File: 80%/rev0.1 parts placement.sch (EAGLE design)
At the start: 205 parts, among them J1 USB-B, SW1 CHERRY_MX, SW10 CHERRY_MX, SW11 CHERRY_MX, SW12 CHERRY_MX, SW13 CHERRY_MX, SW14 CHERRY_MX, SW15 CHERRY_MX, SW16 CHERRY_MX, SW17 CHERRY_MX, SW18 CHERRY_MX, SW19 CHERRY_MX, SW2 CHERRY_MX, SW20 CHERRY_MX, SW21 CHERRY_MX, SW22 CHERRY_MX, SW23 CHERRY_MX, SW24 CHERRY_MX, SW25 CHERRY_MX, SW26 CHERRY_MX, SW27 CHERRY_MX, SW28 CHERRY_MX, SW29 CHERRY_MX, SW3 CHERRY_MX, SW30 CHERRY_MX, SW31 CHERRY_MX, SW32 CHERRY_MX, SW33 CHERRY_MX, SW34 CHERRY_MX, SW35 CHERRY_MX, SW36 CHERRY_MX, SW37 CHERRY_MX, SW38 CHERRY_MX, SW39 CHERRY_MX, SW4 CHERRY_MX, SW40 CHERRY_MX, SW41 CHERRY_MX, SW42 CHERRY_MX, SW43 CHERRY_MX, SW44 CHERRY_MX, SW45 CHERRY_MX, SW46 CHERRY_MX, SW47 CHERRY_MX, SW48 CHERRY_MX, SW49 CHERRY_MX, SW5 CHERRY_MX, SW50 CHERRY_MX, SW51 CHERRY_MX, SW52 CHERRY_MX, SW53 CHERRY_MX, SW54 CHERRY_MX, SW55 CHERRY_MX, SW56 CHERRY_MX, SW57 CHERRY_MX, SW58 CHERRY_MX, SW59 CHERRY_MX, SW6 CHERRY_MX, SW60 CHERRY_MX, SW61 CHERRY_MX, SW62 CHERRY_MX, SW63 CHERRY_MX, SW64 CHERRY_MX, SW65 CHERRY_MX, SW66 CHERRY_MX, SW67 CHERRY_MX, SW68 CHERRY_MX, SW69 CHERRY_MX, SW7 CHERRY_MX, SW70 CHERRY_MX, SW71 CHERRY_MX, SW72 CHERRY_MX, SW73 CHERRY_MX, SW74 CHERRY_MX, SW75 CHERRY_MX, SW76 CHERRY_MX, SW77 CHERRY_MX, SW78 CHERRY_MX, SW79 CHERRY_MX, SW8 CHERRY_MX, SW80 CHERRY_MX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

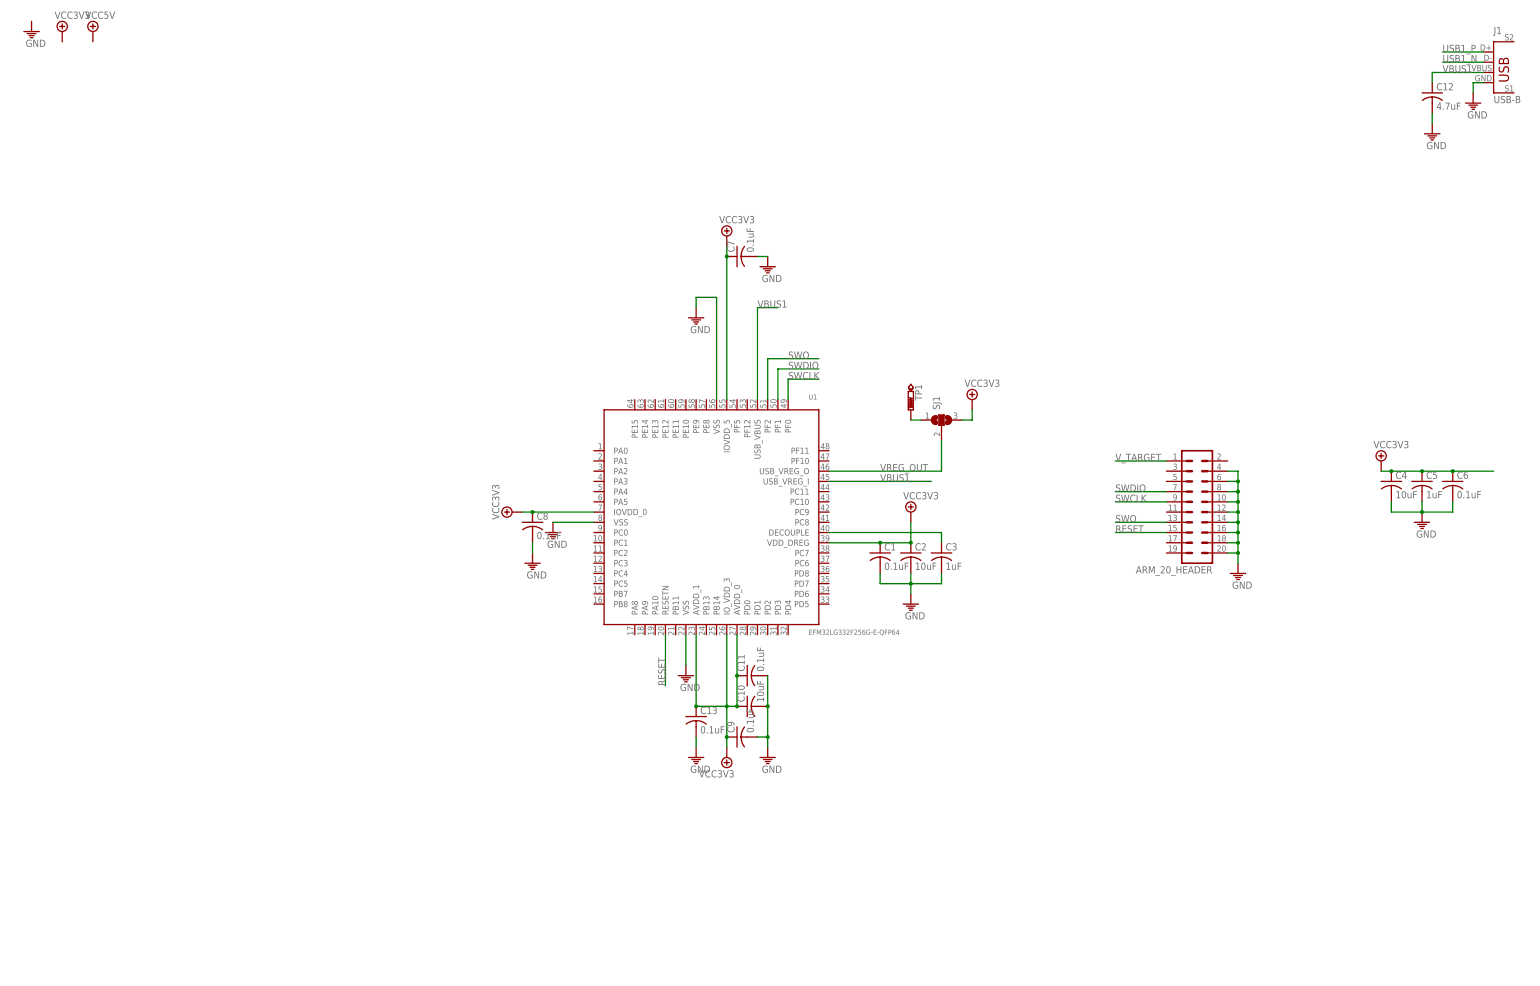
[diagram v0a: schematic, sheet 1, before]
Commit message: changed MCU
changed MCU to a silicon labs MCU. EFM32. need to design power management and we will be groovy!
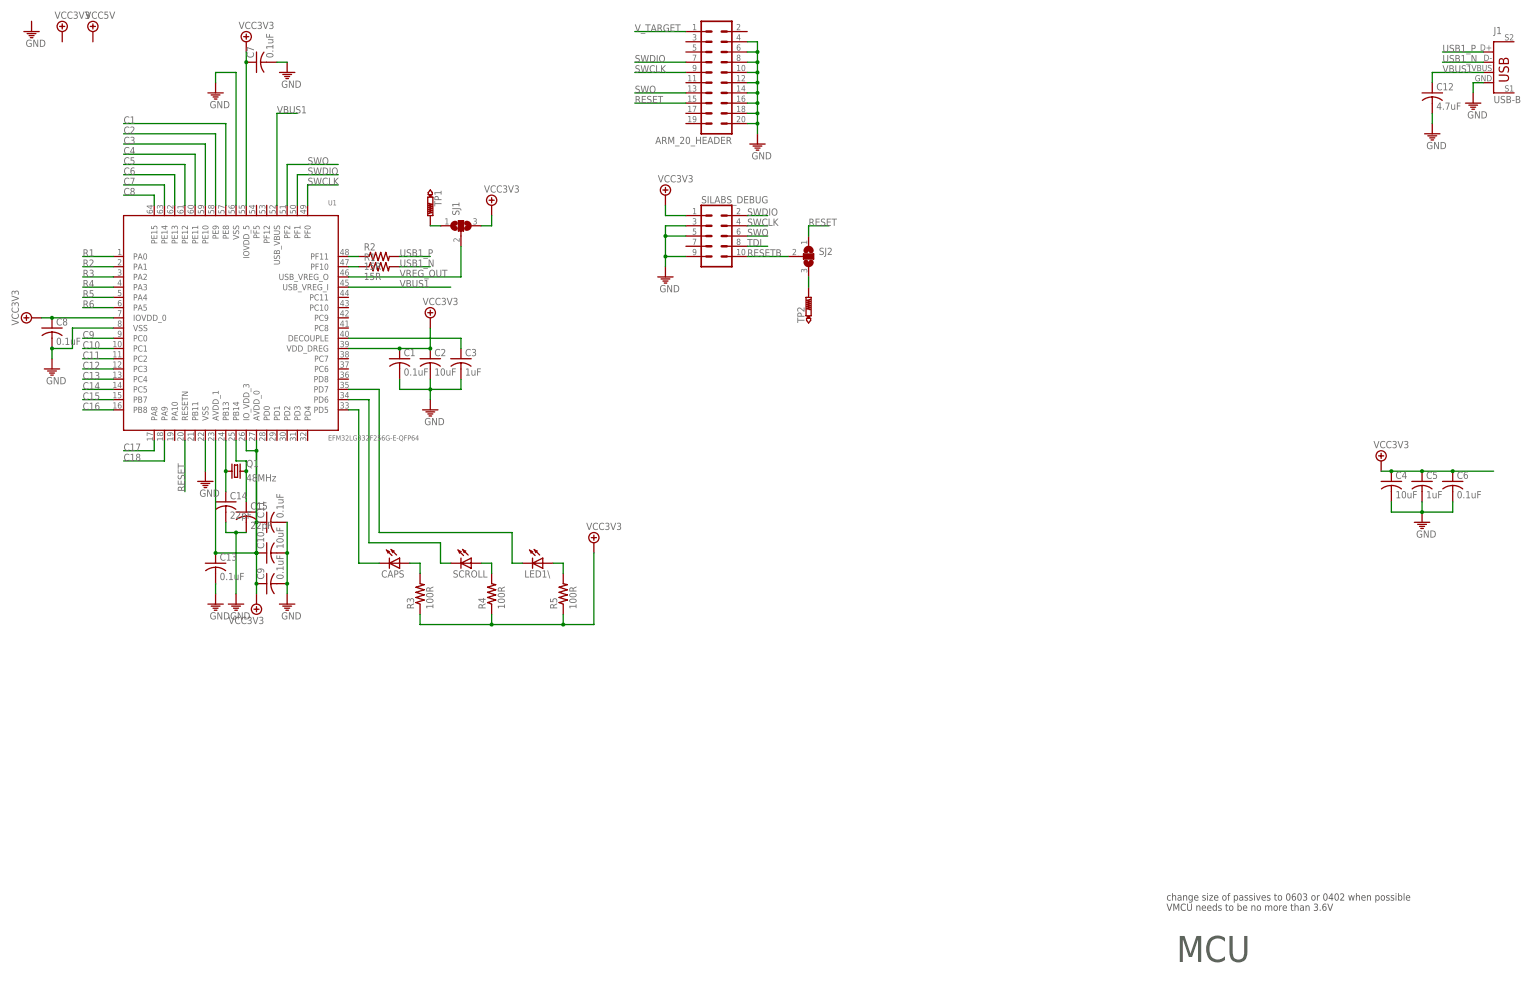
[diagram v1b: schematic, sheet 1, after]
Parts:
- added C14, C15: 22pF, resistor:C-USC0402
- added Q1: 48MHz, adafruit:CRYSTALCTS406
- added R1, R2: 15R, resistor:R-US_R0402
- added R3, R4, R5: 100R, resistor:R-US_R0402
- added SILABS_DEBUG: (no value), SparkFun-Connectors:CONN_05X2SHD_LOCK
- added SJ2: (no value), jumper:SJ2W
- added TP2: PTR1B2,54, testpad:PTR1B2,54
- C1, C11, C13, C3, C5, C6, C7, C8, C9: device resistor:C-USC0805 -> resistor:C-USC0402
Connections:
- removed net N$30: SW13.1, SW30.1, SW48.1, SW66.1, SW80.1
- removed net N$31: SW14.1, SW31.1, SW49.1, SW67.1, SW81.1
- removed net N$32: SW15.1, SW32.1, SW50.1
- removed net N$33: SW16.1, SW33.1, SW51.1
- removed net N$34: SW17.1, SW34.1, SW52.1
- removed net N$35: SW35.1, SW53.1
- new net 1_N: R1.1, U1.PF10
- new net 1_P: R2.1, U1.PF11
- new net C10: SW10.1, SW27.1, SW45.1, SW63.1, SW77.1, SW91.1, U1.PC1
- new net C11: SW11.1, SW28.1, SW46.1, SW64.1, SW78.1, SW92.1, U1.PC2
- new net C12: SW12.1, SW29.1, SW47.1, SW65.1, SW79.1, U1.PC3
- new net C13: SW13.1, SW30.1, SW48.1, SW66.1, SW80.1, U1.PC4
- new net C14: SW14.1, SW31.1, SW49.1, SW67.1, SW81.1, U1.PC5
- new net C15: SW15.1, SW32.1, SW50.1, U1.PB7
- new net C16: SW16.1, SW33.1, SW51.1, U1.PB8
- new net C17: SW17.1, SW34.1, SW52.1, U1.PA8
- new net C18: SW35.1, SW53.1, U1.PA9
- new net C7: SW24.1, SW42.1, SW60.1, SW7.1, SW74.1, SW88.1, U1.PE14
- new net C8: SW25.1, SW43.1, SW61.1, SW75.1, SW8.1, SW89.1, U1.PE15
- new net C9: SW26.1, SW44.1, SW62.1, SW76.1, SW9.1, SW90.1, U1.PC0
- new net N$3: C15.1, Q1.2, U1.PB14
- new net N$4: C14.1, Q1.1, U1.PB13
- new net N$5: SJ2.3, TP2.TP
- new net RESETB: SILABS_DEBUG.10, SJ2.2
- new net TDI: SILABS_DEBUG.8
- net C1: now also U1.PE8
- net C2: now also U1.PE9
- net C3: now also U1.PE10
- net C4: now also U1.PE11
- net C5: now also U1.PE12
- net C6: now also U1.PE13
- net GND: now also C14.2, C15.2, SILABS_DEBUG.3, SILABS_DEBUG.5, SILABS_DEBUG.9
- net N$24: now also CAPS.A, R3.2; no longer SW24.1, SW42.1, SW60.1, SW7.1, SW74.1, SW88.1
- net N$25: now also R4.2, SCROLL.A; no longer SW25.1, SW43.1, SW61.1, SW75.1, SW8.1, SW89.1
- net N$26: now also LED1\.A, R5.2; no longer SW44.1, SW62.1, SW76.1, SW9.1, SW90.1
- net N$27: now also CAPS.C, U1.PD5; no longer SW10.1, SW27.1, SW45.1, SW63.1, SW77.1, SW91.1
- net N$28: now also SCROLL.C, U1.PD6; no longer SW11.1, SW28.1, SW46.1, SW64.1, SW78.1, SW92.1
- net N$29: now also LED1\.C, U1.PD7; no longer SW12.1, SW29.1, SW47.1, SW65.1, SW79.1
- net R1: now also U1.PA0
- net R2: now also U1.PA1
- net R3: now also U1.PA2
- net R4: now also U1.PA3
- net R5: now also U1.PA4
- net R6: now also U1.PA5
- net RESET: now also SJ2.1
- net SWCLK: now also SILABS_DEBUG.4
- net SWDIO: now also SILABS_DEBUG.2
- net SWO: now also SILABS_DEBUG.6
- net USB1_N: now also R1.2
- net USB1_P: now also R2.2
- net VCC3V3: now also R3.1, R4.1, R5.1, SILABS_DEBUG.1
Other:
- note added: "MCU"
- note added: "VMCU needs to be no more than 3.6V"
- note added: "change size of passives to 0603 or 0402 when possible"
- moved on the sheet: ARM_20_HEADER, C1, C10, C11, C13, C2, C3, C7, C8, C9, SJ1, TP1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

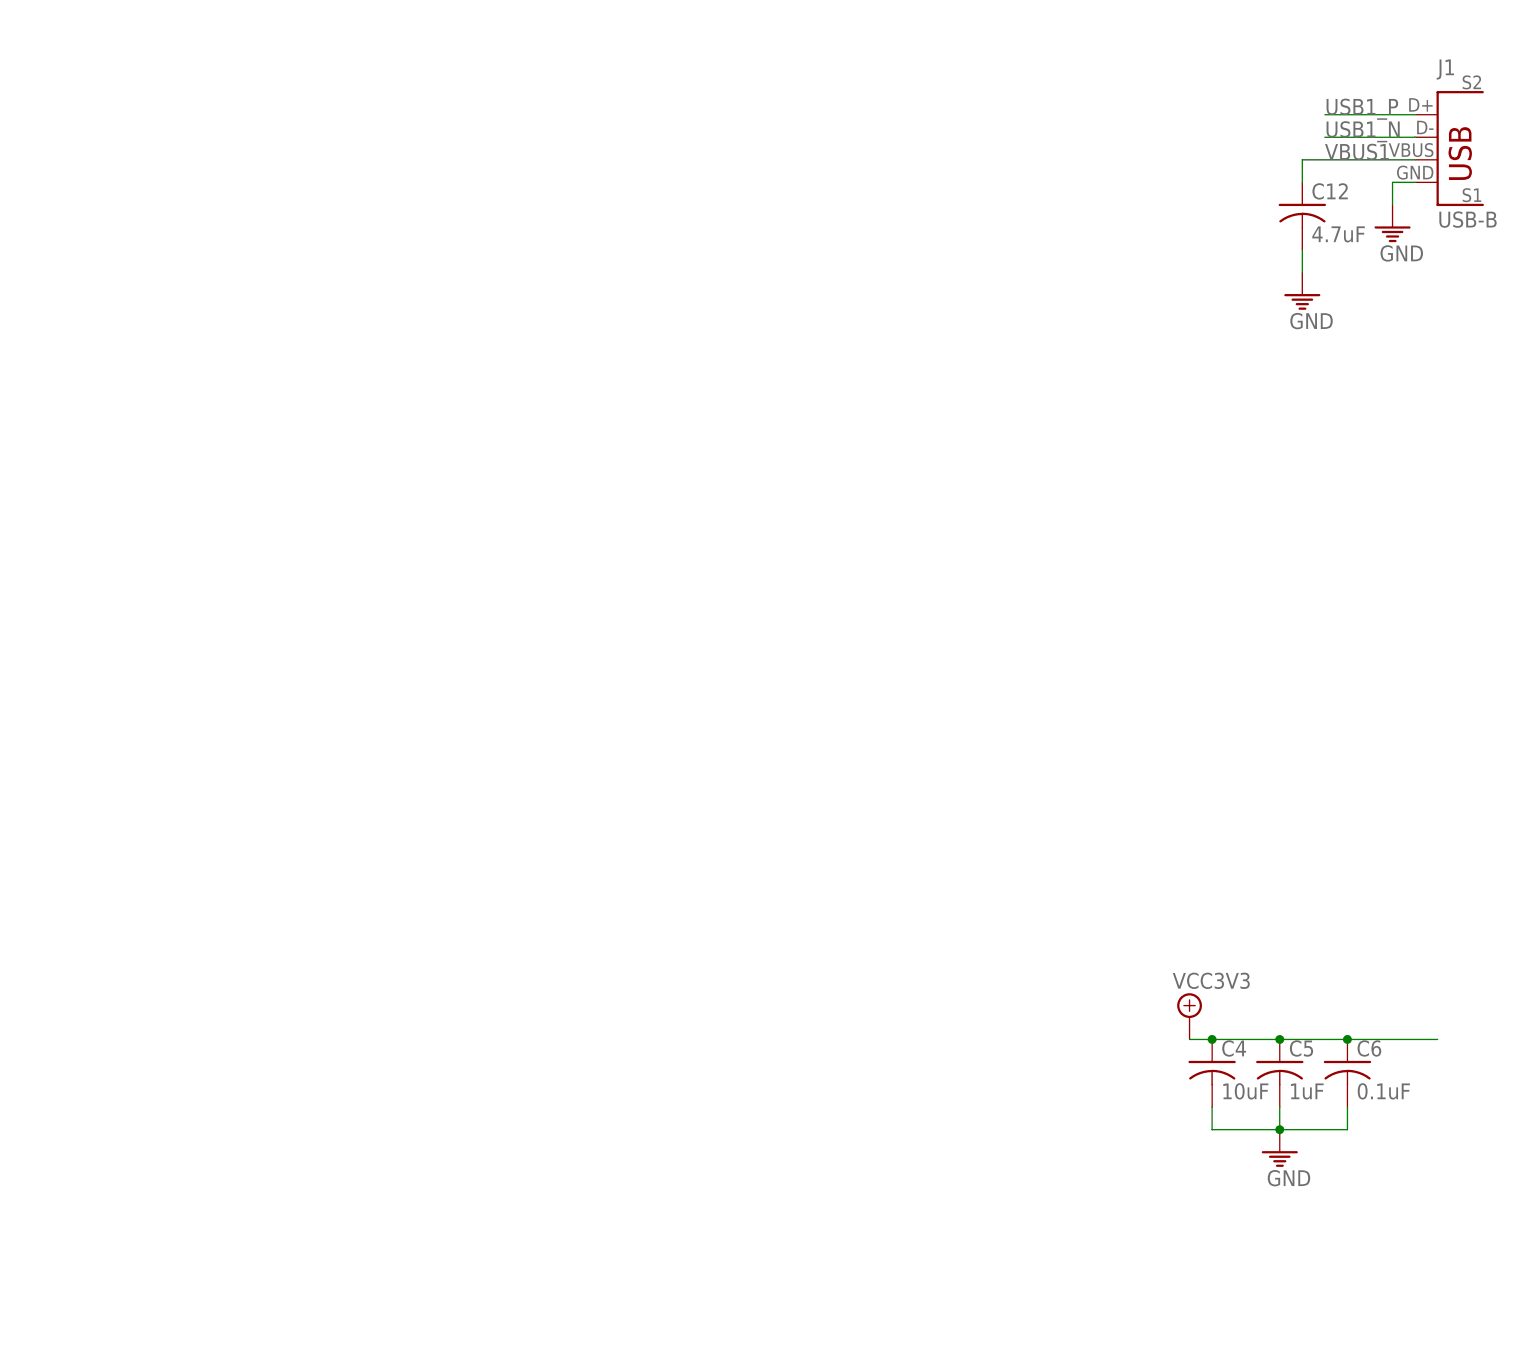
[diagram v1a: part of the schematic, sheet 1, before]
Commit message: cleaned up a little
added power routing
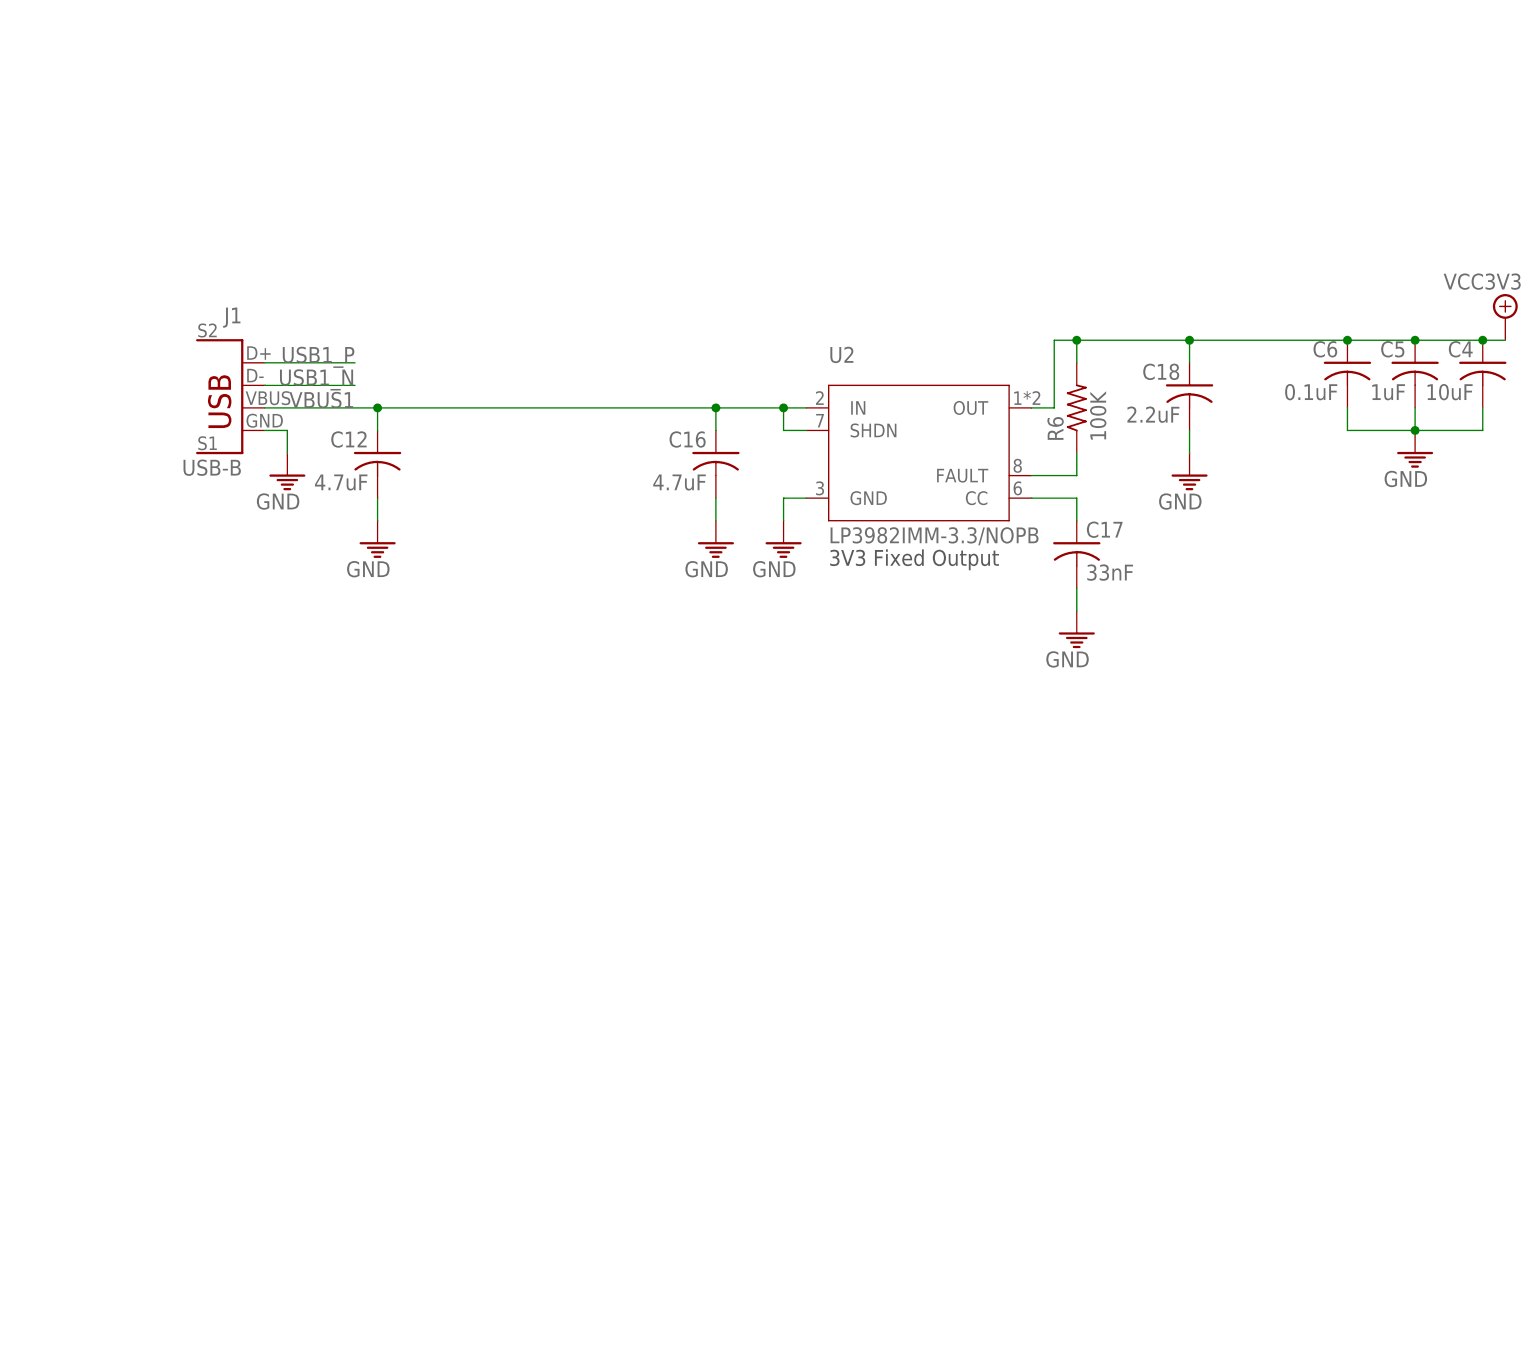
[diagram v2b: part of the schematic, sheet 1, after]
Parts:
- added C16: 4.7uF, resistor:C-USC0805
- added C17: 33nF, resistor:C-USC0402
- added C18: 2.2uF, resistor:C-USC0805
- added R6: 100K, resistor:R-US_R0402
- added U2: LP3982IMM-3.3/NOPB, clackboard_lib:LP3982IMM-3.3/NOPB
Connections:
- new net N$31: C17.1, U2.CC
- new net N$32: R6.1, U2.FAULT
- net GND: now also C16.2, C17.2, C18.2, U2.GND
- net VBUS1: now also C16.1, U2.IN, U2.SHDN
- net VCC3V3: now also C18.1, R6.2, U2.OUT
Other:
- note added: "3V3 Fixed Output"
- moved on the sheet: C12, C4, C5, C6, J1
